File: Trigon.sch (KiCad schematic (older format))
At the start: 70 parts, among them J1 USB_C_Receptacle_USB2.0, SW1 SW_Push, SW2 Rotary_Encoder_Switch, U1 ATmega32U4-AU, Y1 16MHz

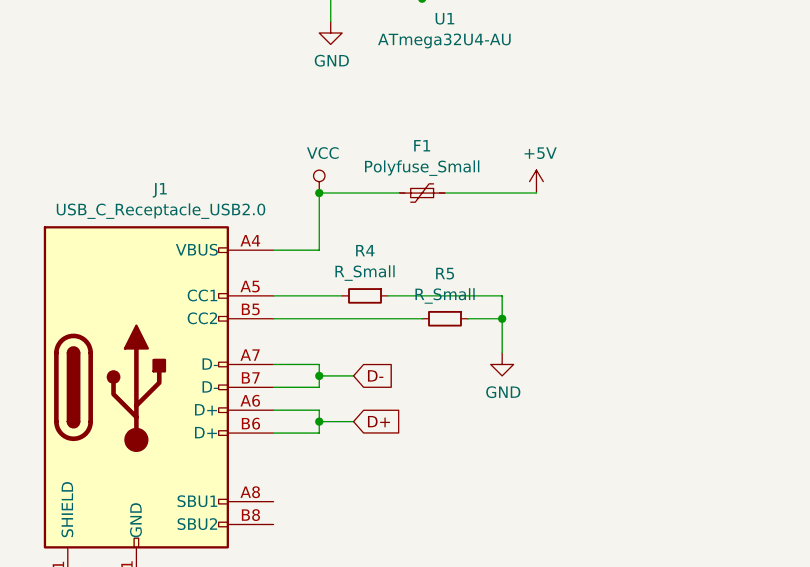
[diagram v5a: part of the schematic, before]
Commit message: cleaning up ground plane for solder mask layer
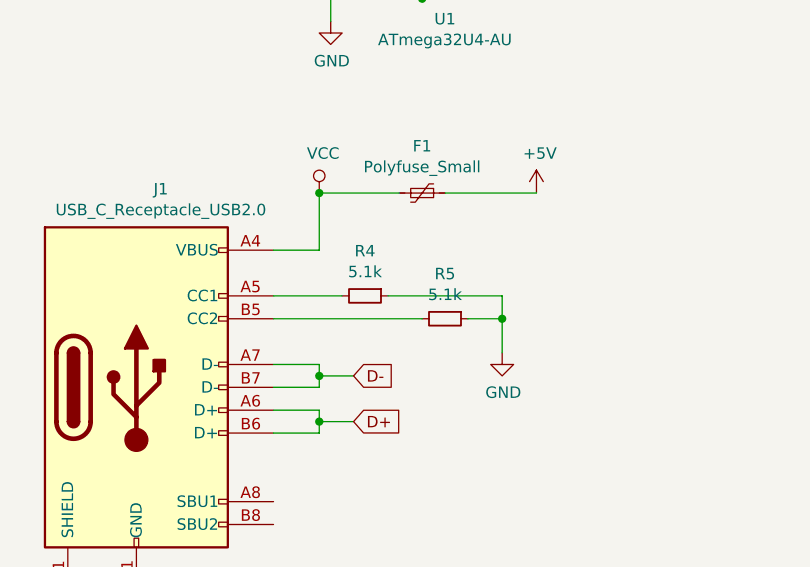
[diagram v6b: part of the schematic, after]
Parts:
- C7: footprint Diode_SMD:D_SOD-123 -> Capacitor_SMD:C_0805_2012Metric
- R4, R5: value R_Small -> 5.1k
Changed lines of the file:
@@
 F 0 "C7" H 6092 6646 50  0000 L CNN
 F 1 "10uF" H 6092 6555 50  0000 L CNN
-F 2 "Diode_SMD:D_SOD-123" H 6000 6600 50  0001 C CNN
+F 2 "Capacitor_SMD:C_0805_2012Metric" H 6000 6600 50  0001 C CNN
 F 3 "~" H 6000 6600 50  0001 C CNN
 	1    6000 6600
@@
 P 2300 6000
 F 0 "R4" V 2104 6000 50  0000 C CNN
-F 1 "R_Small" V 2195 6000 50  0000 C CNN
+F 1 "5.1k" V 2195 6000 50  0000 C CNN
 F 2 "Resistor_SMD:R_0805_2012Metric" H 2300 6000 50  0001 C CNN
 F 3 "~" H 2300 6000 50  0001 C CNN
@@
 P 2650 6100
 F 0 "R5" V 2454 6100 50  0000 C CNN
-F 1 "R_Small" V 2545 6100 50  0000 C CNN
+F 1 "5.1k" V 2545 6100 50  0000 C CNN
 F 2 "Resistor_SMD:R_0805_2012Metric" H 2650 6100 50  0001 C CNN
 F 3 "~" H 2650 6100 50  0001 C CNN

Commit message: new usb connector'
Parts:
- removed J1: USB_C_Receptacle_USB2.0, Connector_USB:USB_C_Receptacle_Palconn_UTC16-G, symbol Connector:USB_C_Receptacle_USB2.0
- added J1: TYPE-C-31-M12_13, acheron_Connectors:TYPE-C-31-M-12, symbol acheronSymbols:TYPE-C-31-M12_13
- F1: value Polyfuse_Small -> 500mA
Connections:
- net D+: now also J1.A6 (D+), J1.B6 (D+)
- net D-: now also J1.A7 (D-), J1.B7 (D-)
- net GND: now also J1.A1 (GND), J1.B1 (GND), J1.S (SHIELD)
- net VCC: now also J1.A4 (VBUS), J1.B4 (VBUS)
- net at R4.2: now also J1.A5 (CC1)
- net at R5.2: now also J1.B5 (CC2)
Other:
- moved on the sheet: C1, C2, C3, F1, R1, R2, R3, R4, R5, R6, SW1, U1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

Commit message: Checkpoint
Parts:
- SW2: footprint Rotary_Encoder:RotaryEncoder_Alps_EC12E-Switch_Vertical_H20mm -> Keebio-Parts:RotaryEncoder_Alps_EC11E-Switch_Vertical_H20mm
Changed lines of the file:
@@
 F 0 "SW2" H 10100 2683 50  0000 C CNN
 F 1 "Rotary_Encoder_Switch" H 10100 2774 50  0000 C CNN
-F 2 "Rotary_Encoder:RotaryEncoder_Alps_EC12E-Switch_Vertical_H20mm" H 9950 3210 50  0001 C CNN
+F 2 "Keebio-Parts:RotaryEncoder_Alps_EC11E-Switch_Vertical_H20mm" H 9950 3210 50  0001 C CNN
 F 3 "~" H 10100 3310 50  0001 C CNN
 	1    10100 3050
